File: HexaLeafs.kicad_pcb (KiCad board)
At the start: 2 copper layers, 104 x 90 mm, 25 parts, among them J1 Conn_01x04, J2 Conn_01x04

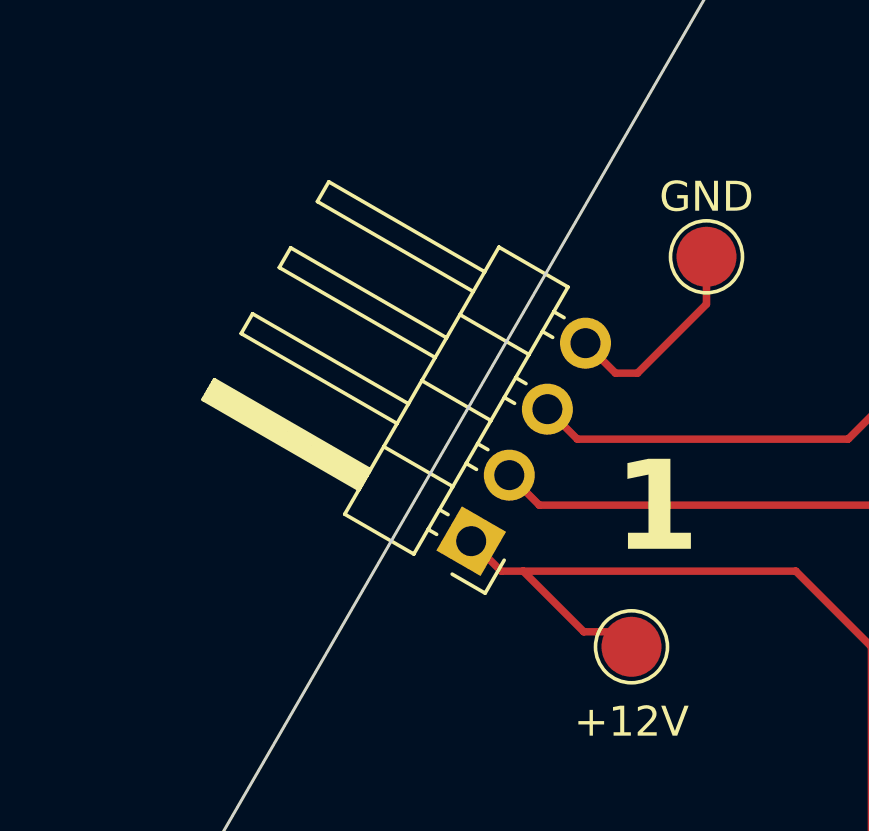
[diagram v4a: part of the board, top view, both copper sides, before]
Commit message: Align male connector
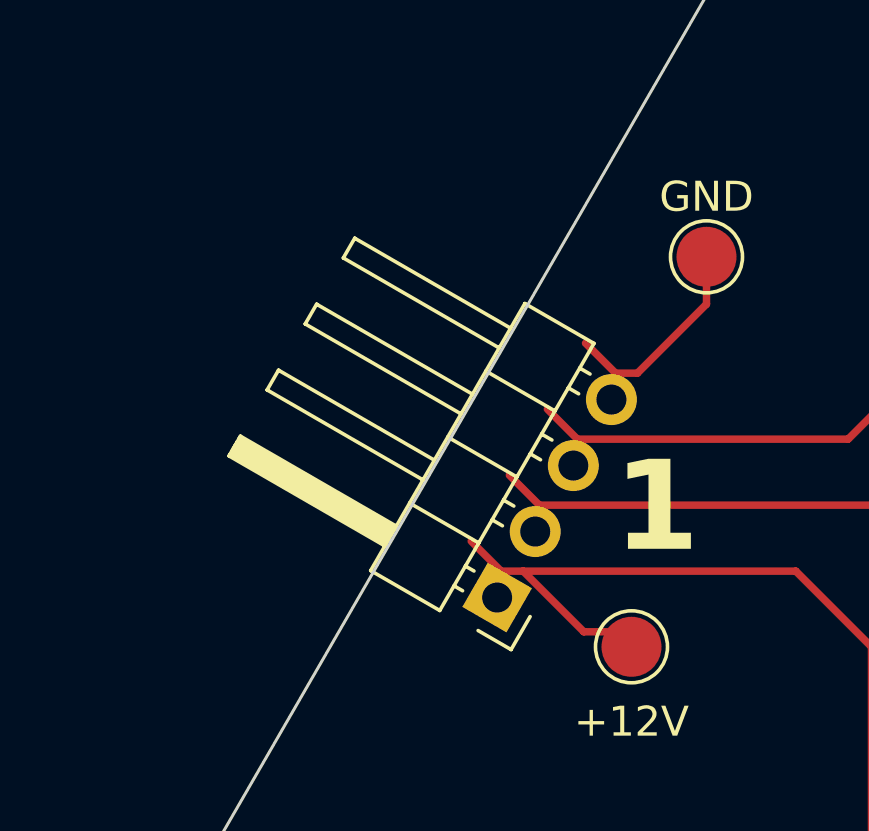
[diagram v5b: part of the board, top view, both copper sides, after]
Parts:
- moved J1 3.11 mm to (52.8, 48.6)

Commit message: WIP
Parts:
- renumbered J2 to J3, J2 to J4, J2 to J5, J2 to J6
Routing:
- net GND: track 62.3 -> 259.3 mm
- net 2nd In: track 43.2 -> 234.2 mm
- net Out2: track 45.8 -> 89.6 mm
- net Out6: track 57.1 -> 13.8 mm
- net Out5: track 42.4 -> 13.5 mm, vias 1 -> 0
- net +12V: track 409.4 -> 425.6 mm

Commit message: Corrected Plug assignment
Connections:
- J3 pad 3: Out2 -> Out3
- J4 pad 3: Out2 -> Out4
- J5 pad 3: Out2 -> Out5
- J6 pad 3: Out2 -> Out6
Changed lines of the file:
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@@
 			(layers "*.Cu" "*.Mask")
 			(remove_unused_layers no)
-			(net 17 "Out2")
+			(net 22 "Out6")
 			(pinfunction "Pin_3")
 			(pintype "passive")
@@
 			(layers "*.Cu" "*.Mask")
 			(remove_unused_layers no)
-			(net 17 "Out2")
+			(net 19 "Out3")
 			(pinfunction "Pin_3")
 			(pintype "passive")
@@
 		)
 		(fp_text user "${REFERENCE}"
-			(at -5.775 0 360)
+			(at -5.775 0 0)
 			(layer "F.Fab")
 			(effects
@@
 			(layers "*.Cu" "*.Mask")
 			(remove_unused_layers no)
-			(net 17 "Out2")
+			(net 21 "Out5")
 			(pinfunction "Pin_3")
 			(pintype "passive")
@@
 			(layers "*.Cu" "*.Mask")
 			(remove_unused_layers no)
-			(net 17 "Out2")
+			(net 20 "Out4")
 			(pinfunction "Pin_3")
 			(pintype "passive")

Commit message: WIP
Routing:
- net 2nd In: track 234.2 -> 149.2 mm
- net Out4: track 52.6 -> 53.5 mm
- net +12V: track 425.6 -> 425.0 mm
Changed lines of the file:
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@@
-	)
-	(segment
-		(start 120.34319 87.189557)
-		(end 119.909729 86.756096)
-		(width 0.25)
-		(layer "F.Cu")
-		(net 2)
 	)
 	(segment
@@
 	)
 	(segment
-		(start 120.218713 56.718713)
-		(end 122 58.5)
-		(width 0.25)
-		(layer "F.Cu")
-		(net 18)
-	)
-	(segment
 		(start 87.1457 105.400159)
 		(end 87.1457 104.1457)
@@
 	)
 	(segment
-		(start 123.5 88)
-		(end 123.119628 88.380372)
-		(width 0.25)
-		(layer "F.Cu")
-		(net 18)
-	)
-	(segment
-		(start 122 58.5)
-		(end 122 59.5)
-		(width 0.25)
-		(layer "F.Cu")
-		(net 18)
-	)
-	(segment
 		(start 87.1457 106.6457)
 		(end 87.1457 105.400159)
@@
 	)
 	(segment
-		(start 123.119628 88.380372)
-		(end 119.164835 88.380372)
-		(width 0.25)
-		(layer "F.Cu")
-		(net 18)
-	)
-	(segment
 		(start 60 103)
 		(end 60 98.5)
@@
 	)
 	(segment
-		(start 120.218713 52.357216)
-		(end 120.218713 56.718713)
-		(width 0.25)
-		(layer "F.Cu")
-		(net 18)
-	)
-	(segment
 		(start 115 100.5)
 		(end 105.5 110)
@@
 	)
 	(segment
-		(start 92.264097 35.5)
-		(end 113.5 35.5)
-		(width 0.25)
-		(layer "F.Cu")
-		(net 18)
-	)
-	(segment
 		(start 54.077233 88.5)
 		(end 56.396565 86.180668)
@@
 	)
 	(segment
-		(start 122 59.5)
-		(end 123.5 61)
-		(width 0.25)
-		(layer "F.Cu")
-		(net 18)
-	)
-	(segment
-		(start 113.5 35.5)
-		(end 120.434835 42.434835)
-		(width 0.25)
-		(layer "F.Cu")
-		(net 18)
-	)
-	(segment
-		(start 89.6857 32.921603)
-		(end 92.264097 35.5)
-		(width 0.25)
-		(layer "F.Cu")
-		(net 18)
-	)
-	(segment
-		(start 120.434835 42.434835)
-		(end 120.434835 52.141094)
-		(width 0.25)
-		(layer "F.Cu")
-		(net 18)
-	)
-	(segment
-		(start 123.5 61)
-		(end 123.5 88)
-		(width 0.25)
-		(layer "F.Cu")
-		(net 18)
-	)
-	(segment
-		(start 118.177678 85.756096)
-		(end 118.909729 85.756096)
-		(width 0.25)
-		(layer "B.Cu")
-		(net 18)
-	)
-	(segment
-		(start 118.177678 85.756096)
+		(start 119.164835 88.380372)
+		(end 119.164835 86.743253)
+		(width 0.25)
+		(layer "B.Cu")
+		(net 18)
+	)
+	(segment
+		(start 119.164835 86.743253)
 		(end 101.675685 69.254103)
-		(width 0.25)
-		(layer "B.Cu")
-		(net 18)
-	)
-	(segment
-		(start 118.909729 85.756096)
-		(end 119.909729 86.756096)
 		(width 0.25)
 		(layer "B.Cu")
@@
 	)
 	(segment
-		(start 118.649729 51.256392)
-		(end 119.649729 50.256392)
+		(start 87.94819 75.749103)
+		(end 87.94819 65.689103)
+		(width 0.25)
+		(layer "B.Cu")
+		(net 19)
+	)
+	(segment
+		(start 119.164835 50.009235)
+		(end 119.164835 49.94139)
+		(width 0.25)
+		(layer "B.Cu")
+		(net 19)
+	)
+	(segment
+		(start 90.64819 62.989103)
+		(end 106.184967 62.989103)
 		(width 0.25)
 		(layer "B.Cu")
@@
 	)
 	(segment
-		(start 106.184967 62.989103)
-		(end 117.917678 51.256392)
-		(width 0.25)
-		(layer "B.Cu")
-		(net 19)
-	)
-	(segment
-		(start 117.917678 51.256392)
-		(end 118.649729 51.256392)
-		(width 0.25)
-		(layer "B.Cu")
-		(net 19)
-	)
-	(segment
-		(start 87.94819 75.749103)
-		(end 87.94819 65.689103)
-		(width 0.25)
-		(layer "B.Cu")
-		(net 19)
-	)
-	(segment
-		(start 90.64819 62.989103)
-		(end 106.184967 62.989103)
-		(width 0.25)
-		(layer "B.Cu")
-		(net 19)
-	)
-	(segment
 		(start 87.94819 65.689103)
 		(end 89.07319 64.564103)
@@
 	)
 	(segment
-		(start 99.330389 63.439103)
-		(end 119.447678 83.556392)
+		(start 106.184967 62.989103)
+		(end 119.164835 50.009235)
+		(width 0.25)
+		(layer "B.Cu")
+		(net 19)
+	)
+	(segment
+		(start 91.61319 64.564103)
+		(end 92.73819 63.439103)
 		(width 0.25)
 		(layer "B.Cu")
@@
 	)
 	(segment
-		(start 119.447678 83.556392)
-		(end 120.179729 83.556392)
+		(start 92.73819 63.439103)
+		(end 99.330389 63.439103)
 		(width 0.25)
 		(layer "B.Cu")
@@
 	)
 	(segment
-		(start 92.73819 63.439103)
-		(end 99.330389 63.439103)
-		(width 0.25)
-		(layer "B.Cu")
-		(net 20)
-	)
-	(segment
-		(start 91.61319 64.564103)
-		(end 92.73819 63.439103)
-		(width 0.25)
-		(layer "B.Cu")
-		(net 20)
-	)
-	(segment
 		(start 91.61319 76.874103)
 		(end 90.19819 75.459103)
@@
 	)
 	(segment
-		(start 120.179729 83.556392)
-		(end 121.179729 84.556392)
+		(start 99.330389 63.439103)
+		(end 120.434835 84.543549)
 		(width 0.25)
 		(layer "B.Cu")
@@
 		(start 91.49069 76.874103)
 		(end 91.34319 77.021603)
+		(width 0.25)
+		(layer "B.Cu")
+		(net 20)
+	)
+	(segment
+		(start 120.434835 84.543549)
+		(end 120.434835 86.180668)
 		(width 0.25)
 		(layer "B.Cu")
@@
 		(min_thickness 0.25)
 		(filled_areas_thickness no)
-		(fill
+		(fill yes
 			(thermal_gap 0.5)
 			(thermal_bridge_width 0.5)
@@
 		(min_thickness 0.25)
 		(filled_areas_thickness no)
-		(fill
+		(fill yes
 			(thermal_gap 0.5)
 			(thermal_bridge_width 0.5)
